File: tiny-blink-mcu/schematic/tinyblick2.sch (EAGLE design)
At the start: 57 parts, among them IC1 SE555D, IC2 LM358D, IC3 74LS595D, IC4 74LS595D, J1 USB-MICROB

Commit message: Updated schematic and board layout
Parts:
- removed C3: 10nF, adafruit:C-USC0603
- removed C4: 100nF, adafruit:C-USC0603
- removed C6: 5nF, adafruit:C-USC0603
- removed C7: 0uF, adafruit:C-USC0603
- removed C9: 4.7uF, adafruit:C-USC0603
- removed IC1: SE555D, adafruit:SE555D
- removed IC2: LM358D, linear:LM358D
- removed R10: 10K, adafruit:R-US_R0603
- removed R11: 1K, adafruit:R-US_R0603
- removed R12: 5.1K, adafruit:R-US_R0603
- added C12: 10nF, adafruit:C-USC0603
- added S1: MOMENTARY-SWITCH-SPST-SMD-4.6X2.8MM, SparkFun-Switches:MOMENTARY-SWITCH-SPST-SMD-4.6X2.8MM
- added TP1, TP2, TP3, TP4, TP5, TP6: TPB1,27, testpad:TPB1,27
- R1: value 10K -> (none)
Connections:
- removed net CLK: IC1.Q, IC2A.-IN, IC3.SCK, IC4.SCK
- removed net CLR: IC3.RCK, IC4.RCK, U$2.PB3(ADC3)
- removed net N$26: IC2A.+IN, R1.1, R10.2
- removed net N$3: IC1.DIS, R11.1, R12.2
- removed net N$30: C6.2, IC1.CV
- removed net N$6: C7.1, C9.1, IC1.THR, IC1.TR, R12.1
- new net LATCH: C12.2, IC3.RCK, IC4.RCK, TP1.TP, U$2.PB3(ADC3)
- new net NRES: TP3.TP, U$2.PB5(NRES)
- new net PB4: R1.1, S1.2, TP2.TP, U$2.PB4(ADC2)
- net +3V3: no longer C3.1, C4.1, IC1.R, IC1.V+, IC2P.V+, R11.2
- net GND: now also C12.1, S1.1; no longer C3.2, C4.2, C6.1, C7.2, C9.2, IC1.GND, IC2P.V-, R10.1
- net PWM: now also TP6.TP
- net RCLK: now also IC3.SCK, IC4.SCK, TP5.TP; no longer IC2A.OUT
- net SER: now also TP4.TP
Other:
- note removed: "2Hz"
- moved on the sheet: GND, R1, VCC

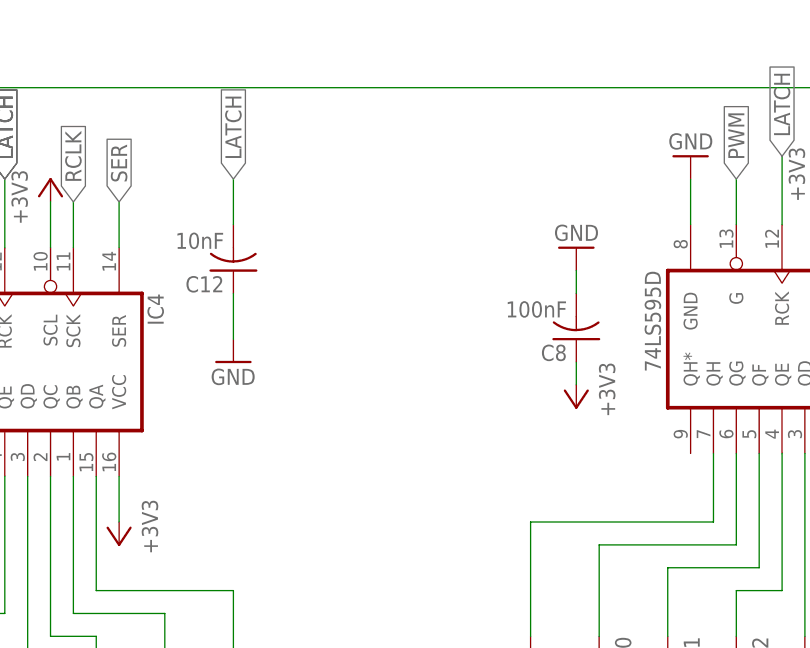
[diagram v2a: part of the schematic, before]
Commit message: Relocated files, removed unused files, updated christmas and clock board and other changes
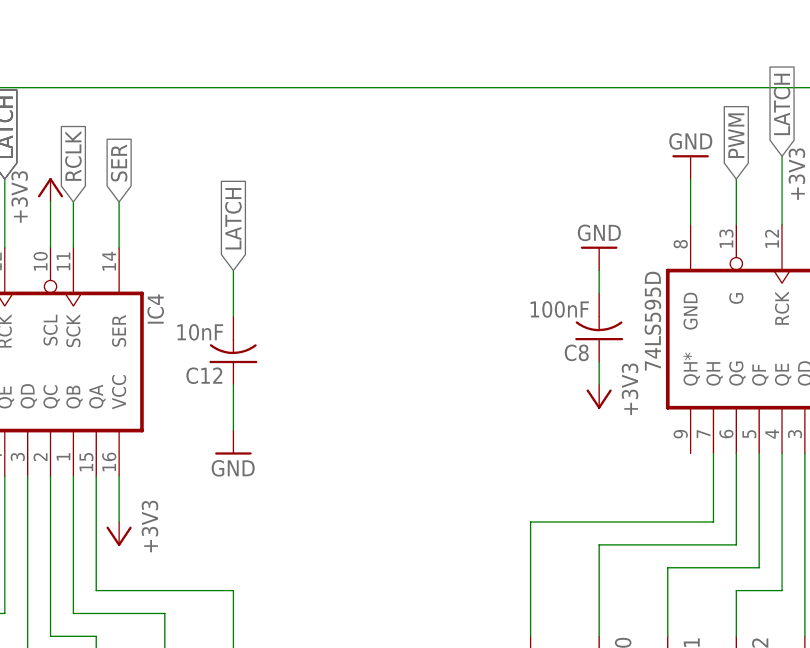
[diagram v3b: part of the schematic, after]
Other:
- moved on the sheet: C12, C8
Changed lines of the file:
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@@
 <attribute name="VALUE" x="589.28" y="152.4" size="1.778" layer="96"/>
 </instance>
-<instance part="C8" gate="G$1" x="568.96" y="218.44" smashed="yes" rot="R180">
-<attribute name="NAME" x="567.944" y="217.805" size="1.778" layer="95" rot="R180"/>
-<attribute name="VALUE" x="567.944" y="222.631" size="1.778" layer="96" rot="R180"/>
-</instance>
-<instance part="GND17" gate="1" x="568.96" y="228.6" smashed="yes" rot="R180">
-<attribute name="VALUE" x="571.5" y="231.14" size="1.778" layer="96" rot="R180"/>
-</instance>
-<instance part="+3V12" gate="G$1" x="568.96" y="210.82" smashed="yes" rot="R180">
-<attribute name="VALUE" x="571.5" y="215.9" size="1.778" layer="96" rot="R270"/>
+<instance part="C8" gate="G$1" x="571.5" y="218.44" smashed="yes" rot="R180">
+<attribute name="NAME" x="570.484" y="217.805" size="1.778" layer="95" rot="R180"/>
+<attribute name="VALUE" x="570.484" y="222.631" size="1.778" layer="96" rot="R180"/>
+</instance>
+<instance part="GND17" gate="1" x="571.5" y="228.6" smashed="yes" rot="R180">
+<attribute name="VALUE" x="574.04" y="231.14" size="1.778" layer="96" rot="R180"/>
+</instance>
+<instance part="+3V12" gate="G$1" x="571.5" y="210.82" smashed="yes" rot="R180">
+<attribute name="VALUE" x="574.04" y="215.9" size="1.778" layer="96" rot="R270"/>
 </instance>
 <instance part="GND18" gate="1" x="581.66" y="238.76" smashed="yes" rot="R180">
@@
 <attribute name="VALUE" x="490.22" y="111.76" size="1.778" layer="96" rot="R180"/>
 </instance>
-<instance part="C12" gate="G$1" x="530.86" y="226.06" smashed="yes" rot="R180">
-<attribute name="NAME" x="529.844" y="225.425" size="1.778" layer="95" rot="R180"/>
-<attribute name="VALUE" x="529.844" y="230.251" size="1.778" layer="96" rot="R180"/>
-</instance>
-<instance part="GND19" gate="1" x="530.86" y="215.9" smashed="yes">
-<attribute name="VALUE" x="528.32" y="213.36" size="1.778" layer="96"/>
+<instance part="C12" gate="G$1" x="530.86" y="215.9" smashed="yes" rot="R180">
+<attribute name="NAME" x="529.844" y="215.265" size="1.778" layer="95" rot="R180"/>
+<attribute name="VALUE" x="529.844" y="220.091" size="1.778" layer="96" rot="R180"/>
+</instance>
+<instance part="GND19" gate="1" x="530.86" y="205.74" smashed="yes">
+<attribute name="VALUE" x="528.32" y="203.2" size="1.778" layer="96"/>
 </instance>
 <instance part="TP1" gate="G$1" x="414.02" y="157.48" smashed="yes">
@@
 <pinref part="C8" gate="G$1" pin="2"/>
 <pinref part="GND17" gate="1" pin="GND"/>
-<wire x1="568.96" y1="223.52" x2="568.96" y2="226.06" width="0.1524" layer="91"/>
+<wire x1="571.5" y1="223.52" x2="571.5" y2="226.06" width="0.1524" layer="91"/>
 </segment>
 <segment>
@@
 <pinref part="C12" gate="G$1" pin="1"/>
 <pinref part="GND19" gate="1" pin="GND"/>
-<wire x1="530.86" y1="223.52" x2="530.86" y2="218.44" width="0.1524" layer="91"/>
+<wire x1="530.86" y1="213.36" x2="530.86" y2="208.28" width="0.1524" layer="91"/>
 </segment>
 <segment>
@@
 <segment>
 <pinref part="C8" gate="G$1" pin="1"/>
-<wire x1="568.96" y1="215.9" x2="568.96" y2="213.36" width="0.1524" layer="91"/>
+<wire x1="571.5" y1="215.9" x2="571.5" y2="213.36" width="0.1524" layer="91"/>
 <pinref part="+3V12" gate="G$1" pin="+3V3"/>
 </segment>
@@
 <segment>
 <pinref part="C12" gate="G$1" pin="2"/>
-<wire x1="530.86" y1="231.14" x2="530.86" y2="236.22" width="0.1524" layer="91"/>
-<label x="530.86" y="236.22" size="1.778" layer="95" rot="R90" xref="yes"/>
-</segment>
-</net>
+<wire x1="530.86" y1="220.98" x2="530.86" y2="226.06" width="0.1524" layer="91"/>
+<label x="530.86" y="226.06" size="1.778" layer="95" rot="R90" xref="yes"/>
+</segment>
+</net>

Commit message: Removed unused files, update board, code and other changes
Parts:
- removed TP1, TP2, TP3, TP4, TP5, TP6: TPB1,27, testpad:TPB1,27
- added LED17: (no value), led:LEDCHIP-LED0603
- added R10: (no value), adafruit:R-US_R0603
- renumbered VCC to 5V
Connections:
- new net N$2: LED17.C, R10.2
- net GND: now also R10.1
- net LATCH: no longer TP1.TP
- net NRES: now also LED17.A; no longer TP3.TP
- net PB4: no longer TP2.TP
- net PWM: no longer TP6.TP
- net RCLK: no longer TP5.TP
- net SER: no longer TP4.TP
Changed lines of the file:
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@@
 <part name="F1" library="adafruit" deviceset="PTCFUSE" device="-1206"/>
 <part name="LED1" library="led" deviceset="LED" device="CHIP-LED0603"/>
-<part name="VCC" library="wirepad" deviceset="WIREPAD" device="SMD2,54-5,08"/>
+<part name="5V" library="wirepad" deviceset="WIREPAD" device="SMD2,54-5,08"/>
 <part name="GND" library="wirepad" deviceset="WIREPAD" device="SMD2,54-5,08"/>
 <part name="R2" library="adafruit" deviceset="R-US_" device="R0603"/>
@@
 <part name="C12" library="adafruit" deviceset="C-US" device="C0603" value="10nF"/>
 <part name="GND19" library="supply1" library_urn="urn:adsk.eagle:library:371" deviceset="GND" device=""/>
-<part name="TP1" library="testpad" library_urn="urn:adsk.eagle:library:385" deviceset="TP" device="B1,27" package3d_urn="urn:adsk.eagle:package:27944/2"/>
-<part name="TP2" library="testpad" library_urn="urn:adsk.eagle:library:385" deviceset="TP" device="B1,27" package3d_urn="urn:adsk.eagle:package:27944/2"/>
-<part name="TP3" library="testpad" library_urn="urn:adsk.eagle:library:385" deviceset="TP" device="B1,27" package3d_urn="urn:adsk.eagle:package:27944/2"/>
-<part name="TP4" library="testpad" library_urn="urn:adsk.eagle:library:385" deviceset="TP" device="B1,27" package3d_urn="urn:adsk.eagle:package:27944/2"/>
-<part name="TP5" library="testpad" library_urn="urn:adsk.eagle:library:385" deviceset="TP" device="B1,27" package3d_urn="urn:adsk.eagle:package:27944/2"/>
-<part name="TP6" library="testpad" library_urn="urn:adsk.eagle:library:385" deviceset="TP" device="B1,27" package3d_urn="urn:adsk.eagle:package:27944/2"/>
 <part name="GND2" library="supply1" library_urn="urn:adsk.eagle:library:371" deviceset="GND" device=""/>
 <part name="R1" library="adafruit" deviceset="R-US_" device="R0603"/>
 <part name="+3V2" library="supply1" deviceset="+3V3" device=""/>
 <part name="S1" library="SparkFun-Switches" library_urn="urn:adsk.eagle:library:535" deviceset="MOMENTARY-SWITCH-SPST" device="-SMD-4.6X2.8MM" package3d_urn="urn:adsk.eagle:package:40176/2"/>
+<part name="LED17" library="led" deviceset="LED" device="CHIP-LED0603"/>
+<part name="R10" library="adafruit" deviceset="R-US_" device="R0603"/>
+<part name="GND3" library="supply1" library_urn="urn:adsk.eagle:library:371" deviceset="GND" device=""/>
 </parts>
 <sheets>
@@
 <attribute name="VALUE" x="483.235" y="175.768" size="1.778" layer="96" rot="R90"/>
 </instance>
-<instance part="VCC" gate="G$1" x="444.5" y="162.56" smashed="yes" rot="R270">
+<instance part="5V" gate="G$1" x="444.5" y="162.56" smashed="yes" rot="R270">
 <attribute name="NAME" x="446.3542" y="163.703" size="1.778" layer="95" rot="R270"/>
 </instance>
@@
 <attribute name="VALUE" x="528.32" y="203.2" size="1.778" layer="96"/>
 </instance>
-<instance part="TP1" gate="G$1" x="414.02" y="157.48" smashed="yes">
-<attribute name="NAME" x="412.75" y="158.75" size="1.778" layer="95"/>
-<attribute name="TP_SIGNAL_NAME" x="415.29" y="156.21" size="1.778" layer="97"/>
-</instance>
-<instance part="TP2" gate="G$1" x="421.64" y="157.48" smashed="yes">
-<attribute name="NAME" x="420.37" y="158.75" size="1.778" layer="95"/>
-<attribute name="TP_SIGNAL_NAME" x="422.91" y="156.21" size="1.778" layer="97"/>
-</instance>
-<instance part="TP3" gate="G$1" x="429.26" y="157.48" smashed="yes">
-<attribute name="NAME" x="427.99" y="158.75" size="1.778" layer="95"/>
-<attribute name="TP_SIGNAL_NAME" x="430.53" y="156.21" size="1.778" layer="97"/>
-</instance>
-<instance part="TP4" gate="G$1" x="406.4" y="157.48" smashed="yes">
-<attribute name="NAME" x="405.13" y="158.75" size="1.778" layer="95"/>
-<attribute name="TP_SIGNAL_NAME" x="407.67" y="156.21" size="1.778" layer="97"/>
-</instance>
-<instance part="TP5" gate="G$1" x="398.78" y="157.48" smashed="yes">
-<attribute name="NAME" x="397.51" y="158.75" size="1.778" layer="95"/>
-<attribute name="TP_SIGNAL_NAME" x="400.05" y="156.21" size="1.778" layer="97"/>
-</instance>
-<instance part="TP6" gate="G$1" x="391.16" y="157.48" smashed="yes">
-<attribute name="NAME" x="389.89" y="158.75" size="1.778" layer="95"/>
-<attribute name="TP_SIGNAL_NAME" x="392.43" y="156.21" size="1.778" layer="97"/>
-</instance>
 <instance part="GND2" gate="1" x="406.4" y="109.22" smashed="yes" rot="R270">
 <attribute name="VALUE" x="403.86" y="111.76" size="1.778" layer="96" rot="R270"/>
@@
 <attribute name="NAME" x="431.8" y="110.744" size="1.778" layer="95" font="vector" align="bottom-center"/>
 <attribute name="VALUE" x="431.8" y="113.792" size="1.778" layer="96" font="vector" align="top-center"/>
+</instance>
+<instance part="LED17" gate="G$1" x="396.24" y="187.96" smashed="yes">
+<attribute name="NAME" x="399.796" y="183.388" size="1.778" layer="95" rot="R90"/>
+<attribute name="VALUE" x="401.955" y="183.388" size="1.778" layer="96" rot="R90"/>
+</instance>
+<instance part="R10" gate="G$1" x="396.24" y="172.72" smashed="yes" rot="R90">
+<attribute name="NAME" x="394.7414" y="168.91" size="1.778" layer="95" rot="R90"/>
+<attribute name="VALUE" x="399.542" y="168.91" size="1.778" layer="96" rot="R90"/>
+</instance>
+<instance part="GND3" gate="1" x="396.24" y="162.56" smashed="yes">
+<attribute name="VALUE" x="393.7" y="160.02" size="1.778" layer="96"/>
 </instance>
 </instances>
@@
 <net name="VCC" class="0">
 <segment>
-<pinref part="VCC" gate="G$1" pin="P"/>
+<pinref part="5V" gate="G$1" pin="P"/>
 <wire x1="444.5" y1="160.02" x2="444.5" y2="154.94" width="0.1524" layer="91"/>
 <pinref part="P+4" gate="VCC" pin="VCC"/>
@@
 <pinref part="S1" gate="G$1" pin="1"/>
 </segment>
+<segment>
+<pinref part="R10" gate="G$1" pin="1"/>
+<pinref part="GND3" gate="1" pin="GND"/>
+<wire x1="396.24" y1="167.64" x2="396.24" y2="165.1" width="0.1524" layer="91"/>
+</segment>
 </net>
 <net name="RCLK" class="0">
@@
 <wire x1="505.46" y1="101.6" x2="520.7" y2="101.6" width="0.1524" layer="91"/>
 <label x="520.7" y="101.6" size="1.778" layer="95" xref="yes"/>
-</segment>
-<segment>
-<pinref part="TP5" gate="G$1" pin="TP"/>
-<wire x1="398.78" y1="154.94" x2="398.78" y2="147.32" width="0.1524" layer="91"/>
-<label x="398.78" y="147.32" size="1.778" layer="95" rot="R270" xref="yes"/>
 </segment>
 <segment>
@@
 <label x="510.54" y="99.06" size="1.778" layer="95" xref="yes"/>
 </segment>
-<segment>
-<pinref part="TP4" gate="G$1" pin="TP"/>
-<wire x1="406.4" y1="154.94" x2="406.4" y2="147.32" width="0.1524" layer="91"/>
-<label x="406.4" y="147.32" size="1.778" layer="95" rot="R270" xref="yes"/>
-</segment>
 </net>
 <net name="N$9" class="0">
@@
 </segment>
 <segment>
-<pinref part="TP1" gate="G$1" pin="TP"/>
-<wire x1="414.02" y1="154.94" x2="414.02" y2="147.32" width="0.1524" layer="91"/>
-<label x="414.02" y="147.32" size="1.778" layer="95" rot="R270" xref="yes"/>
-</segment>
-<segment>
 <pinref part="C12" gate="G$1" pin="2"/>
 <wire x1="530.86" y1="220.98" x2="530.86" y2="226.06" width="0.1524" layer="91"/>
@@
 <label x="586.74" y="236.22" size="1.778" layer="95" rot="R90" xref="yes"/>
 </segment>
-<segment>
-<pinref part="TP6" gate="G$1" pin="TP"/>
-<wire x1="391.16" y1="154.94" x2="391.16" y2="144.78" width="0.1524" layer="91"/>
-<label x="391.16" y="144.78" size="1.778" layer="95" rot="R270" xref="yes"/>
-</segment>
 </net>
 <net name="NRES" class="0">
@@
 </segment>
 <segment>
-<pinref part="TP3" gate="G$1" pin="TP"/>
-<wire x1="429.26" y1="154.94" x2="429.26" y2="147.32" width="0.1524" layer="91"/>
-<label x="429.26" y="147.32" size="1.778" layer="95" rot="R270" xref="yes"/>
+<pinref part="LED17" gate="G$1" pin="A"/>
+<wire x1="396.24" y1="190.5" x2="396.24" y2="198.12" width="0.1524" layer="91"/>
+<label x="396.24" y="198.12" size="1.778" layer="95" rot="R90" xref="yes"/>
 </segment>
 </net>
@@
 <wire x1="505.46" y1="93.98" x2="515.62" y2="93.98" width="0.1524" layer="91"/>
 <label x="515.62" y="93.98" size="1.778" layer="95" xref="yes"/>
-</segment>
-<segment>
-<pinref part="TP2" gate="G$1" pin="TP"/>
-<wire x1="421.64" y1="154.94" x2="421.64" y2="147.32" width="0.1524" layer="91"/>
-<label x="421.64" y="147.32" size="1.778" layer="95" rot="R270" xref="yes"/>
 </segment>
 <segment>
@@
 </segment>
 </net>
+<net name="N$2" class="0">
+<segment>
+<pinref part="LED17" gate="G$1" pin="C"/>
+<pinref part="R10" gate="G$1" pin="2"/>
+<wire x1="396.24" y1="182.88" x2="396.24" y2="177.8" width="0.1524" layer="91"/>
+</segment>
+</net>

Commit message: Improvement and other changes
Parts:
- C10: value 10nF -> 100nF
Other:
- moved on the sheet: 5V, C10, C12, GND, J1, LED17, R1, R10, S1, U$2
